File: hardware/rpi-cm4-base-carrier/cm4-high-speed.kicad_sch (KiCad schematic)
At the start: 5 parts, among them J4 USB_OTG, U2 TPD2EUSB30

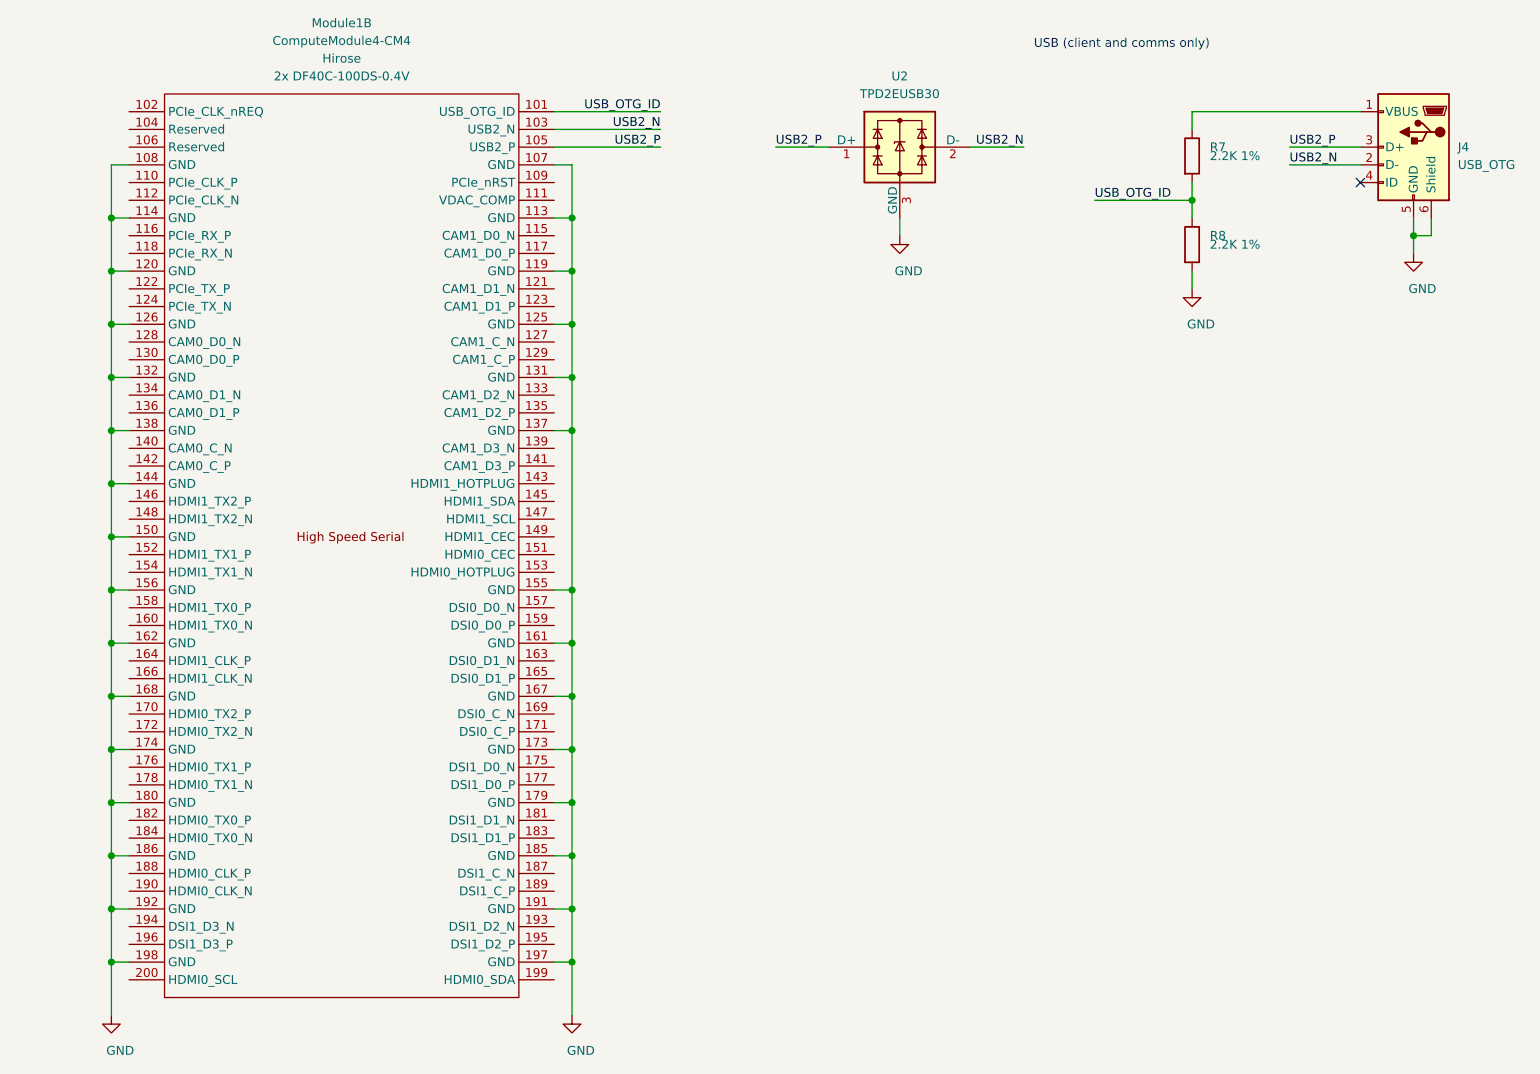
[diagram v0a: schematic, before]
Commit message: schematic changes to add network, hdmi, usbhost and SD
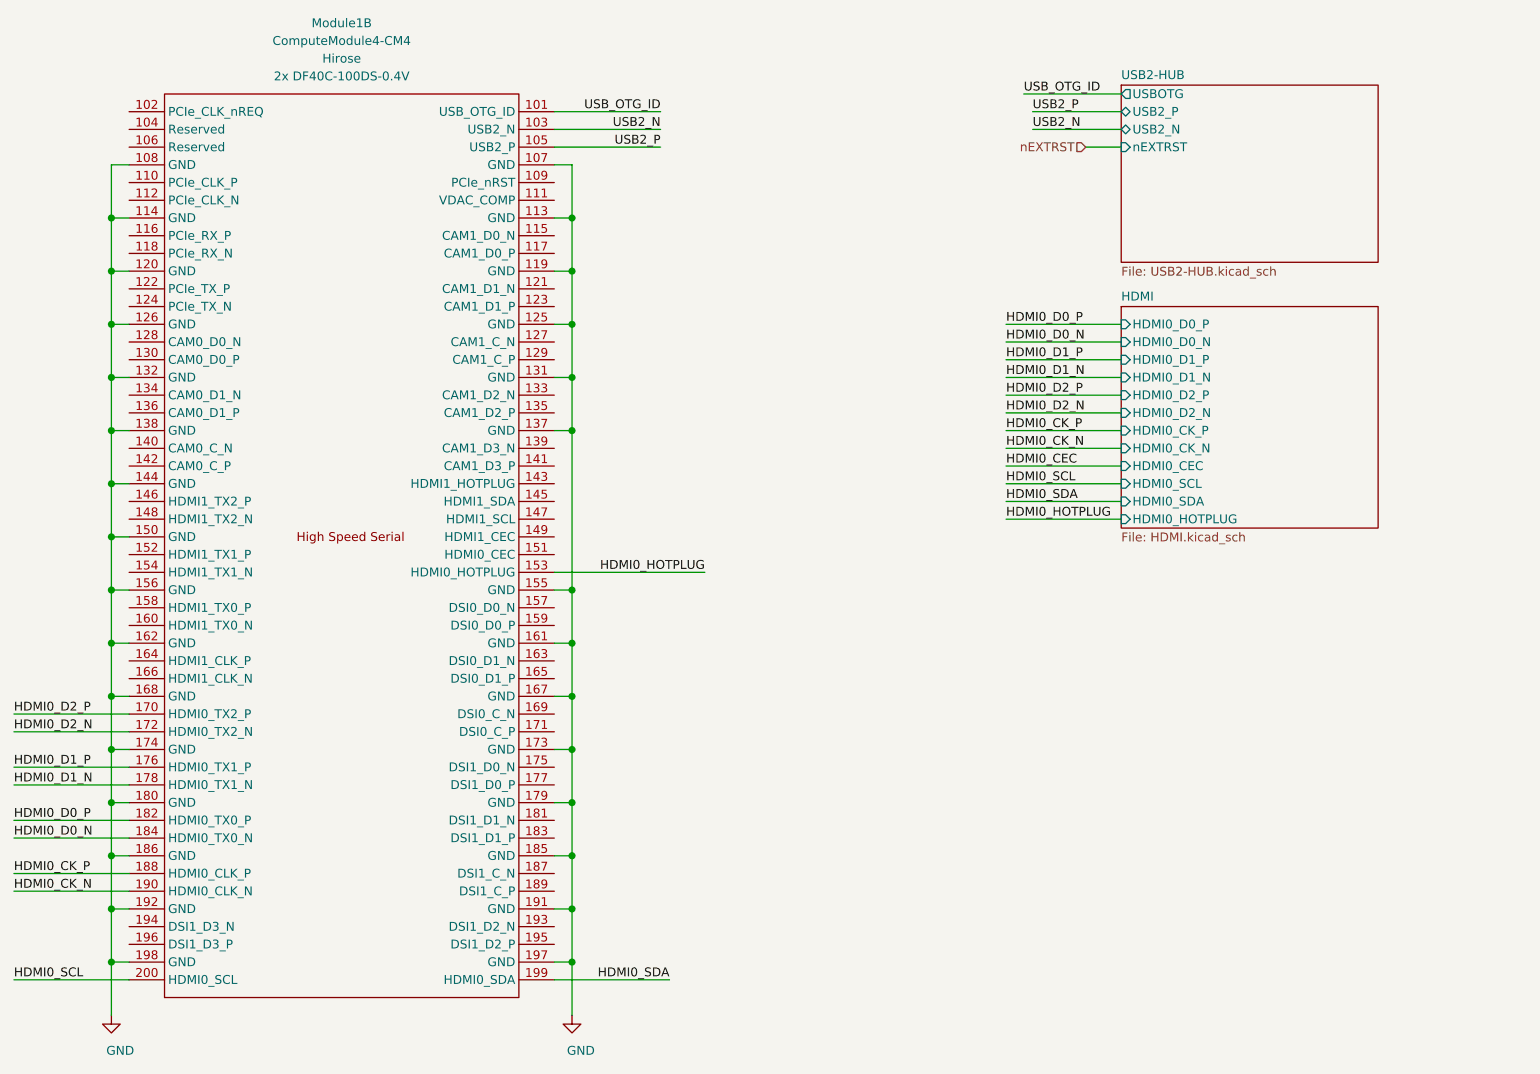
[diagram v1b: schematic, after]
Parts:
- removed J4: USB_OTG, CM4IO:USB_Micro-B_EDAC_UCON00686, symbol Connector:USB_OTG
- removed R7, R8: 2.2K 1%, Resistor_SMD:R_0603_1608Metric_Pad0.98x0.95mm_HandSolder, symbol Device:R
- removed U2: TPD2EUSB30, Package_TO_SOT_SMD:Texas_DRT-3, symbol Power_Protection:TPD2EUSB30
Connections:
- net HDMI0_HOTPLUG: now reaches Module1.153 (HDMI0_HOTPLUG)
- net HDMI0_D2_P: now reaches Module1.170 (HDMI0_TX2_P)
- net HDMI0_D2_N: now reaches Module1.172 (HDMI0_TX2_N)
- net HDMI0_D1_P: now reaches Module1.176 (HDMI0_TX1_P)
- net HDMI0_D1_N: now reaches Module1.178 (HDMI0_TX1_N)
- net HDMI0_D0_P: now reaches Module1.182 (HDMI0_TX0_P)
- net HDMI0_D0_N: now reaches Module1.184 (HDMI0_TX0_N)
- net HDMI0_CK_P: now reaches Module1.188 (HDMI0_CLK_P)
- net HDMI0_CK_N: now reaches Module1.190 (HDMI0_CLK_N)
- net HDMI0_SDA: now reaches Module1.199 (HDMI0_SDA)
- net HDMI0_SCL: now reaches Module1.200 (HDMI0_SCL)
- no-connect marks 1 -> 0
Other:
- added sheet HDMI (HDMI.kicad_sch)
- added sheet USB2-HUB (USB2-HUB.kicad_sch)
- note removed: "USB (client and comms only)"
